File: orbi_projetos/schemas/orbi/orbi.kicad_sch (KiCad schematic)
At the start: 3 parts, among them U1 MPU-6050, U2 ESP32-S2, U3 BMP280

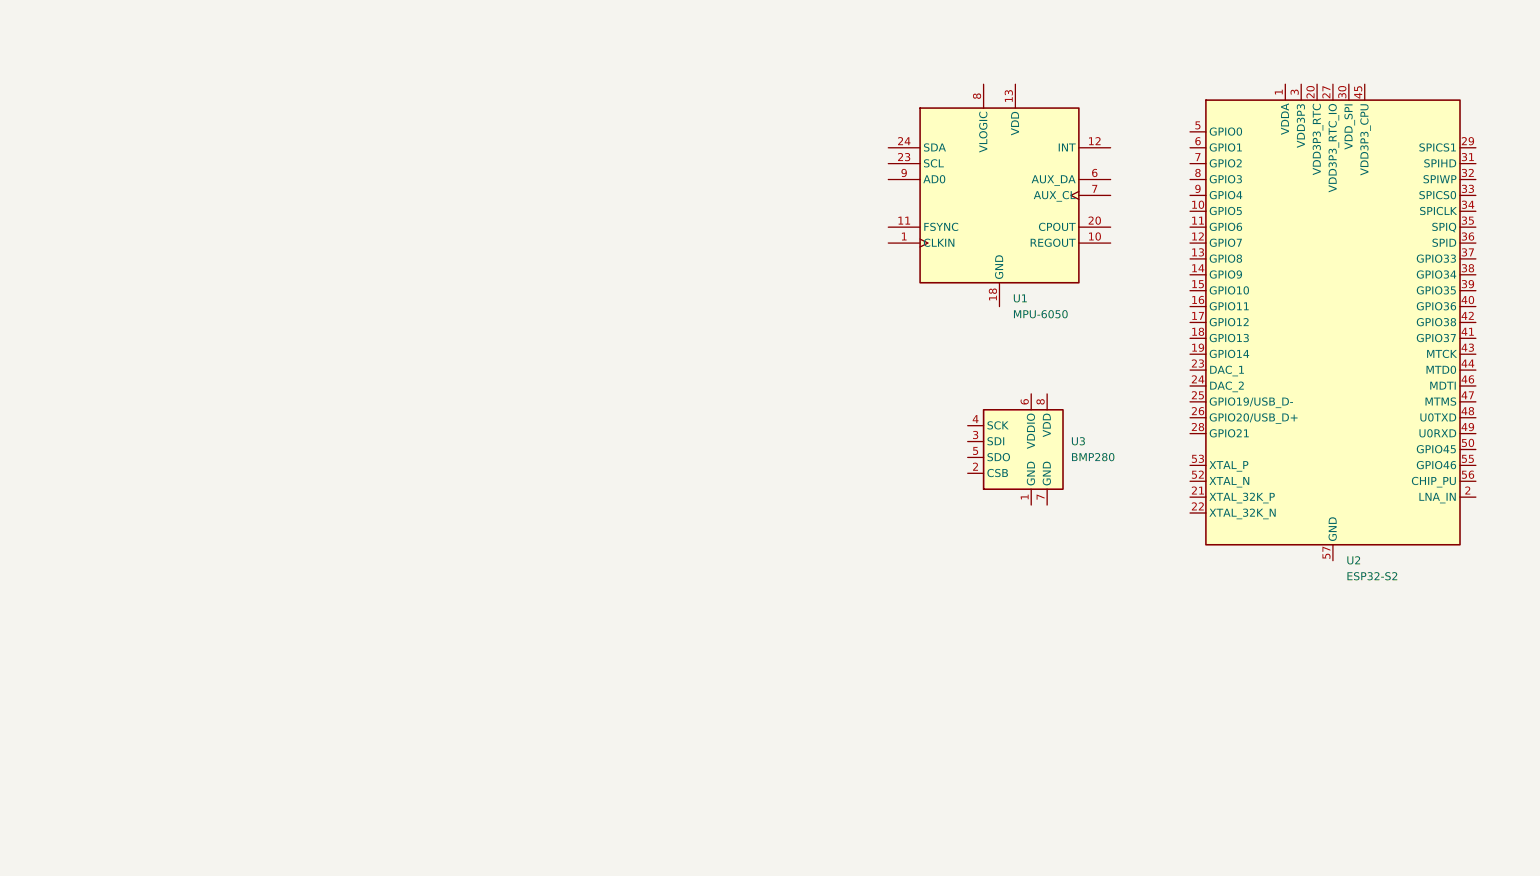
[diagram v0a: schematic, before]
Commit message: Novos Componentes do Projeto
Inserção do USB tipo C e organização de alguns componentes
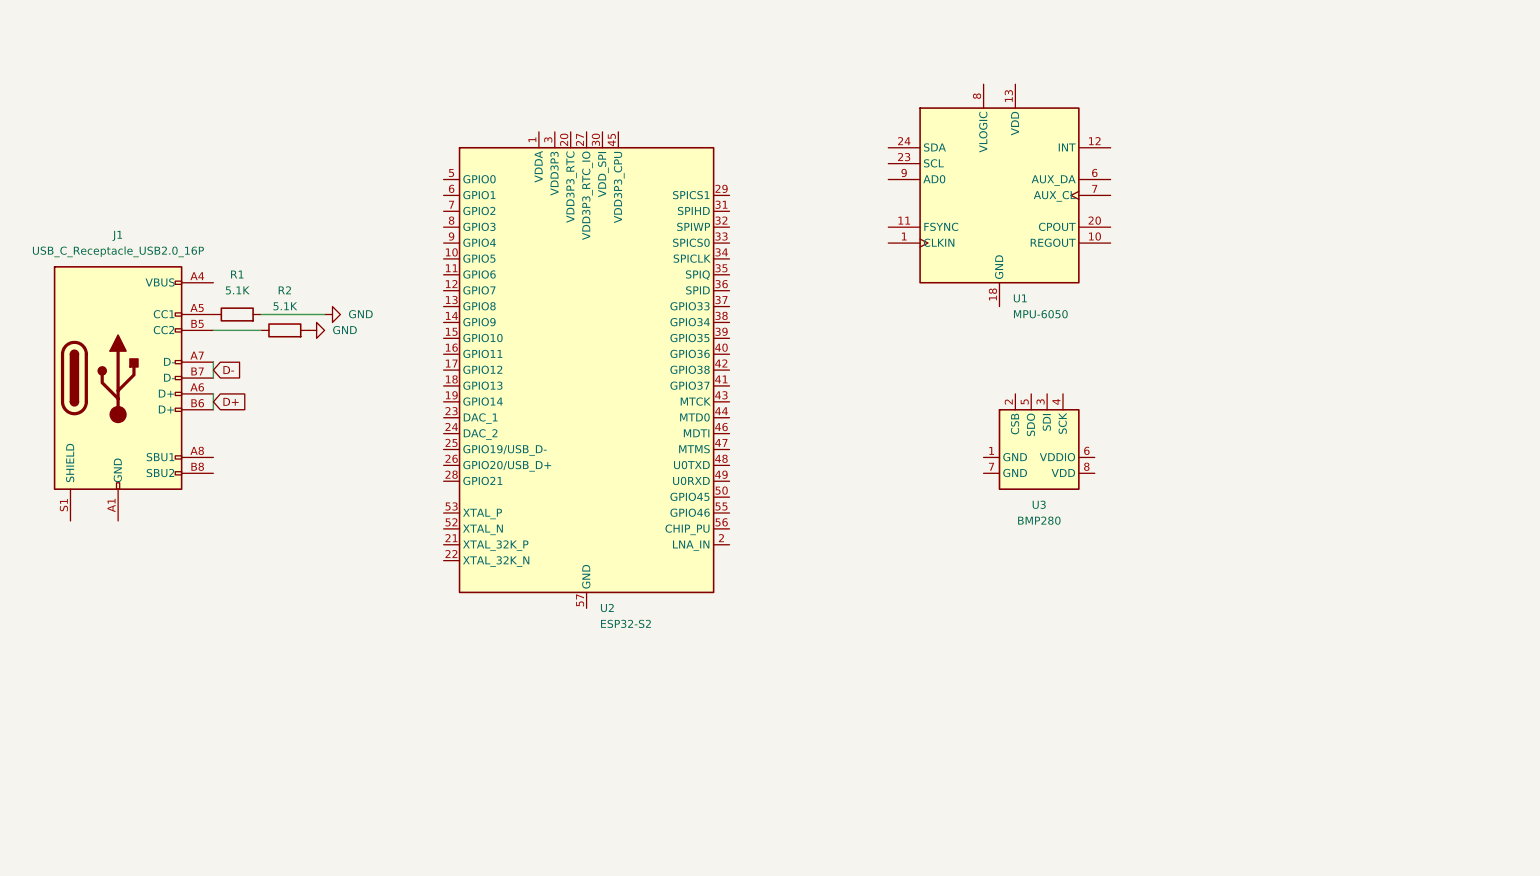
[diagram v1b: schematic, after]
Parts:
- added J1: USB_C_Receptacle_USB2.0_16P, Connector_Card:microSD_HC_Wuerth_693072010801, symbol Connector:USB_C_Receptacle_USB2.0_16P
- added R1, R2: 5.1K, Resistor_SMD:R_0805_2012Metric, symbol Device:R
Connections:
- new net: J1.A1 (GND), J1.A12 (GND), J1.B1 (GND), J1.B12 (GND)
- new net: J1.A4 (VBUS), J1.A9 (VBUS), J1.B4 (VBUS), J1.B9 (VBUS)
- new net: J1.A5 (CC1), R1.1
- new net: J1.B5 (CC2), R2.1
- new net D+: J1.A6 (D+), J1.B6 (D+)
- new net D-: J1.A7 (D-), J1.B7 (D-)
- new net GND: R1.2, R2.2
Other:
- moved on the sheet: U2, U3

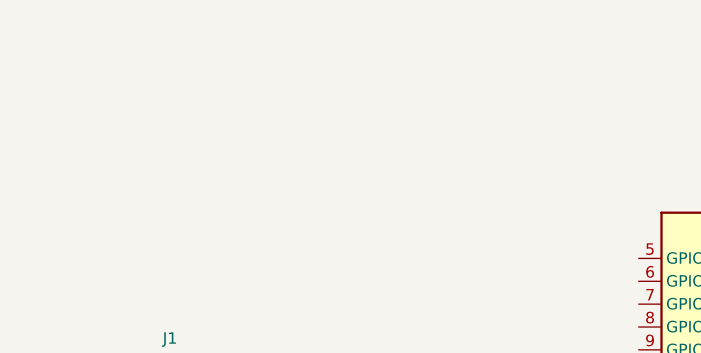
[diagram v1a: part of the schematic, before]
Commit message: Adicionando elemetentos de alimentação energética do projeto
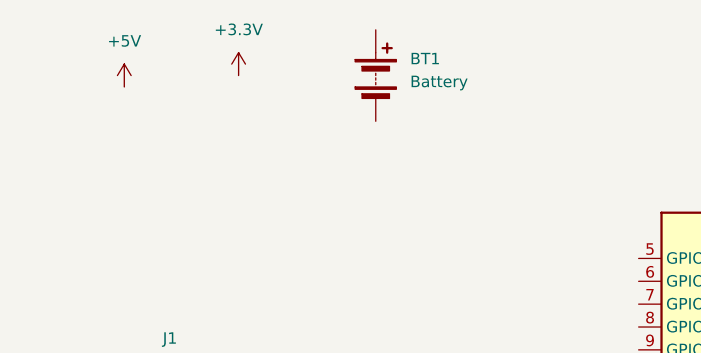
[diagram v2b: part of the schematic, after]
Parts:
- added BT1: Battery, symbol Device:Battery
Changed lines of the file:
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@@
+	)
+	(symbol
+		(lib_id "Device:Battery")
+		(at 55.88 24.13 0)
+		(unit 1)
+		(exclude_from_sim no)
+		(in_bom yes)
+		(on_board yes)
+		(dnp no)
+		(fields_autoplaced yes)
+		(property "Reference" "BT1"
+			(at 59.69 22.2884 0)
+			(effects
+				(font
+					(size 1.27 1.27)
+				)
+				(justify left)
+			)
+		)
+		(property "Value" "Battery"
+			(at 59.69 24.8284 0)
+			(effects
+				(font
+					(size 1.27 1.27)
+				)
+				(justify left)
+			)
+		)
+		(property "Footprint" ""
+			(at 55.88 22.606 90)
+			(effects
+				(font
+					(size 1.27 1.27)
+				)
+				(hide yes)
+			)
+		)
+		(property "Datasheet" "~"
+			(at 55.88 22.606 90)
+			(effects
+				(font
+					(size 1.27 1.27)
+				)
+				(hide yes)
+			)
+		)
+		(property "Description" "Multiple-cell battery"
+			(at 55.88 24.13 0)
+			(effects
+				(font
+					(size 1.27 1.27)
+				)
+				(hide yes)
+			)
+		)
+		(pin "2"
+		)
+		(pin "1"
+		)
+		(instances
+			(project ""
+				(path "/cc5c0dcb-4b74-462c-86de-ed43f1f5f7f0"
+					(reference "BT1")
+					(unit 1)
+				)
+			)
+		)
 	)
 	(symbol
@@
 	)
 	(symbol
+		(lib_id "power:+5V")
+		(at 27.94 25.4 0)
+		(unit 1)
+		(exclude_from_sim no)
+		(in_bom yes)
+		(on_board yes)
+		(dnp no)
+		(fields_autoplaced yes)
+		(property "Reference" "#PWR03"
+			(at 27.94 29.21 0)
+			(effects
+				(font
+					(size 1.27 1.27)
+				)
+				(hide yes)
+			)
+		)
+		(property "Value" "+5V"
+			(at 27.94 20.32 0)
+			(effects
+				(font
+					(size 1.27 1.27)
+				)
+			)
+		)
+		(property "Footprint" ""
+			(at 27.94 25.4 0)
+			(effects
+				(font
+					(size 1.27 1.27)
+				)
+				(hide yes)
+			)
+		)
+		(property "Datasheet" ""
+			(at 27.94 25.4 0)
+			(effects
+				(font
+					(size 1.27 1.27)
+				)
+				(hide yes)
+			)
+		)
+		(property "Description" "Power symbol creates a global label with name \"+5V\""
+			(at 27.94 25.4 0)
+			(effects
+				(font
+					(size 1.27 1.27)
+				)
+				(hide yes)
+			)
+		)
+		(pin "1"
+		)
+		(instances
+			(project ""
+				(path "/cc5c0dcb-4b74-462c-86de-ed43f1f5f7f0"
+					(reference "#PWR03")
+					(unit 1)
+				)
+			)
+		)
+	)
+	(symbol
 		(lib_id "MCU_Espressif:ESP32-S2")
 		(at 107.95 74.93 0)
@@
 					(unit 1)
 				)
+			)
+		)
+	)
+	(symbol
+		(lib_id "power:+3.3V")
+		(at 40.64 24.13 0)
+		(unit 1)
+		(exclude_from_sim no)
+		(in_bom yes)
+		(on_board yes)
+		(dnp no)
+		(fields_autoplaced yes)
+		(property "Reference" "#PWR04"
+			(at 40.64 27.94 0)
+			(effects
+				(font
+					(size 1.27 1.27)
+				)
+				(hide yes)
+			)
+		)
+		(property "Value" "+3.3V"
+			(at 40.64 19.05 0)
+			(effects
+				(font
+					(size 1.27 1.27)
+				)
+			)
+		)
+		(property "Footprint" ""
+			(at 40.64 24.13 0)
+			(effects
+				(font
+					(size 1.27 1.27)
+				)
+				(hide yes)
+			)
+		)
+		(property "Datasheet" ""
+			(at 40.64 24.13 0)
+			(effects
+				(font
+					(size 1.27 1.27)
+				)
+				(hide yes)
+			)
+		)
+		(property "Description" "Power symbol creates a global label with name \"+3.3V\""
+			(at 40.64 24.13 0)
+			(effects
+				(font
+					(size 1.27 1.27)
+				)
+				(hide yes)
+			)
+		)
+		(pin "1"
+		)
+		(instances
+			(project ""
+				(path "/cc5c0dcb-4b74-462c-86de-ed43f1f5f7f0"
+					(reference "#PWR04")
+					(unit 1)
+				)

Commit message: Inserindo Módulo de GPS no Esquemático
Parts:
- added U4: RXM-GPS-FM, RF_GPS:Linx_RXM-GPS, symbol RF_GPS:RXM-GPS-FM
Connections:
- new net: U4.18 (GND), U4.20 (GND), U4.21 (GND), U4.22 (GND)
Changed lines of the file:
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@@
+	)
+	(symbol
+		(lib_id "RF_GPS:RXM-GPS-FM")
+		(at 46.99 138.43 0)
+		(unit 1)
+		(exclude_from_sim no)
+		(in_bom yes)
+		(on_board yes)
+		(dnp no)
+		(fields_autoplaced yes)
+		(property "Reference" "U4"
+			(at 64.77 132.0098 0)
+			(effects
+				(font
+					(size 1.27 1.27)
+				)
+			)
+		)
+		(property "Value" "RXM-GPS-FM"
+			(at 64.77 134.5498 0)
+			(effects
+				(font
+					(size 1.27 1.27)
+				)
+			)
+		)
+		(property "Footprint" "RF_GPS:Linx_RXM-GPS"
+			(at 59.69 152.4 0)
+			(effects
+				(font
+					(size 1.27 1.27)
+				)
+				(hide yes)
+			)
+		)
+		(property "Datasheet" "https://linxtechnologies.com/wp/wp-content/uploads/rxm-gps-fm.pdf"
+			(at 54.61 146.05 0)
+			(effects
+				(font
+					(size 1.27 1.27)
+				)
+				(hide yes)
+			)
+		)
+		(property "Description" "Module GPS Low Power, 14mA tracking, 22 channels"
+			(at 46.99 138.43 0)
+			(effects
+				(font
+					(size 1.27 1.27)
+				)
+				(hide yes)
+			)
+		)
+		(pin "19"
+		)
+		(pin "8"
+		)
+		(pin "22"
+		)
+		(pin "7"
+		)
+		(pin "13"
+		)
+		(pin "21"
+		)
+		(pin "5"
+		)
+		(pin "1"
+		)
+		(pin "10"
+		)
+		(pin "16"
+		)
+		(pin "14"
+		)
+		(pin "3"
+		)
+		(pin "9"
+		)
+		(pin "18"
+		)
+		(pin "6"
+		)
+		(pin "4"
+		)
+		(pin "11"
+		)
+		(pin "12"
+		)
+		(pin "2"
+		)
+		(pin "20"
+		)
+		(pin "15"
+		)
+		(instances
+			(project ""
+				(path "/cc5c0dcb-4b74-462c-86de-ed43f1f5f7f0"
+					(reference "U4")
+					(unit 1)
+				)
+			)
+		)
 	)
 	(symbol

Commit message: Inserindo novos componentes para funcionar o do ESP com depuração
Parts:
- added C1, C2, C3, C4, C5, C6: C, Capacitor_SMD:C_0201_0603Metric, symbol Device:C
- added R3, R4, R5, R6, R7, R8: R, symbol Device:R
- added SW1, SW2: SW_Push, symbol Switch:SW_Push
- added U5: TLV75801PDRV, Package_SON:WSON-6-1EP_2x2mm_P0.65mm_EP1x1.6mm, symbol Regulator_Linear:TLV75801PDRV
- added U6: D3V3XA4B10LP, Package_DFN_QFN:Diodes_UDFN-10_1.0x2.5mm_P0.5mm, symbol Power_Protection:D3V3XA4B10LP
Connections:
- new net: U5.3 (GND), U5.7 (GND)
- new net: U6.3 (VSS), U6.8 (VSS)
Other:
- moved on the sheet: U1
